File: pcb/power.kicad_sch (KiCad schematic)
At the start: 49 parts, among them U5 REG_LDO_3V3_250mA_TI_LP5907MF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, U7 REG_SW_BOOST_TI_TLV61046ADBV

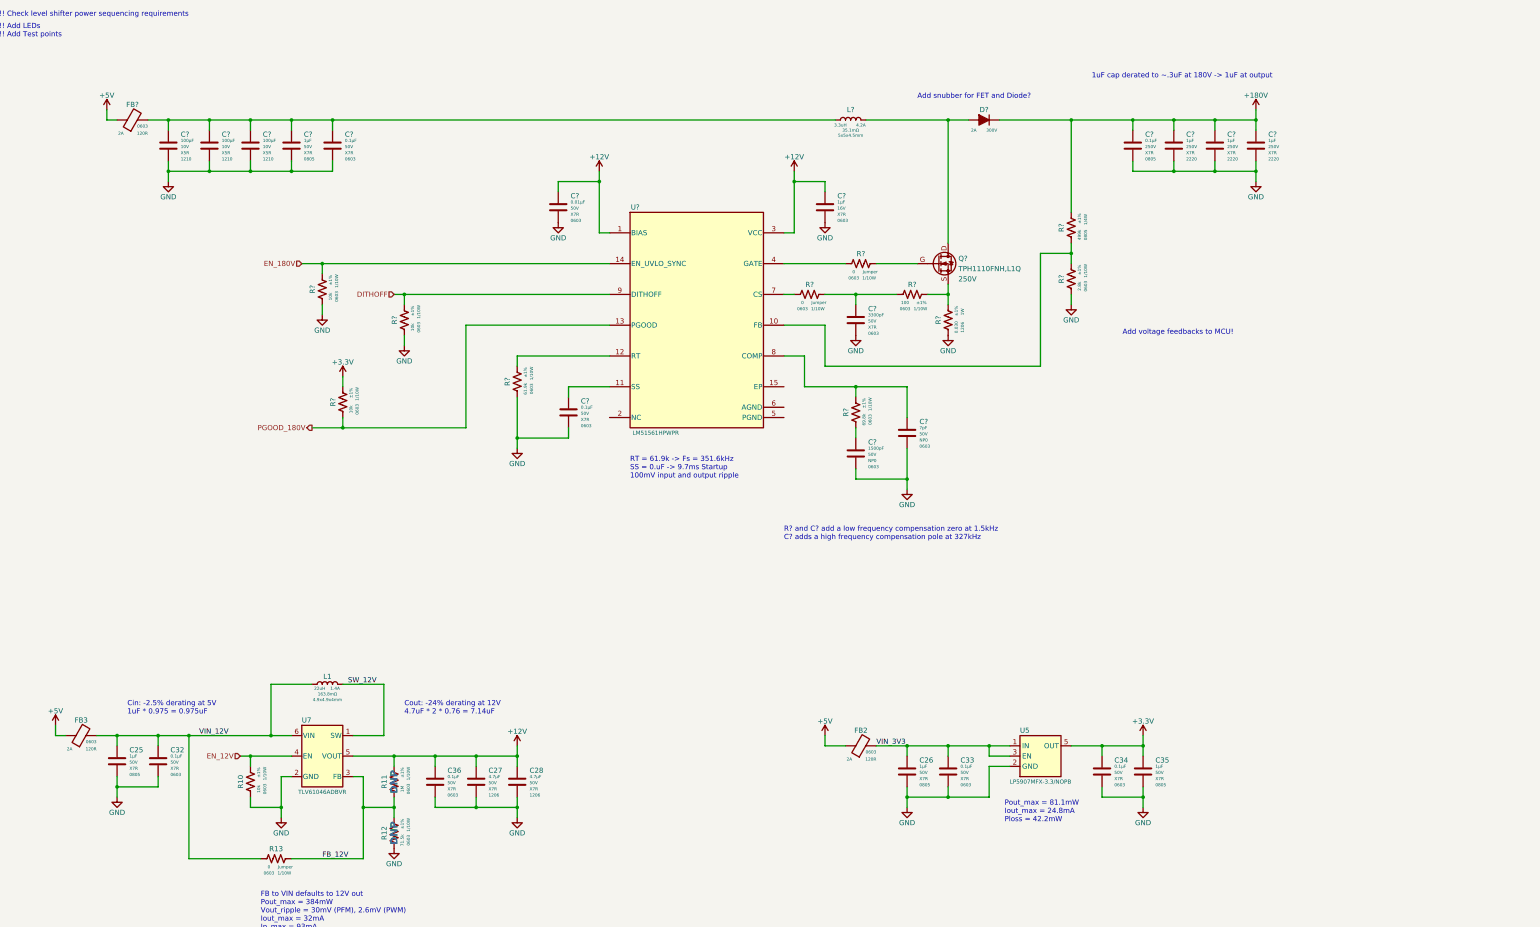
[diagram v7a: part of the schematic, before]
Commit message: Added snubber DNP footprints and named nets on power page.
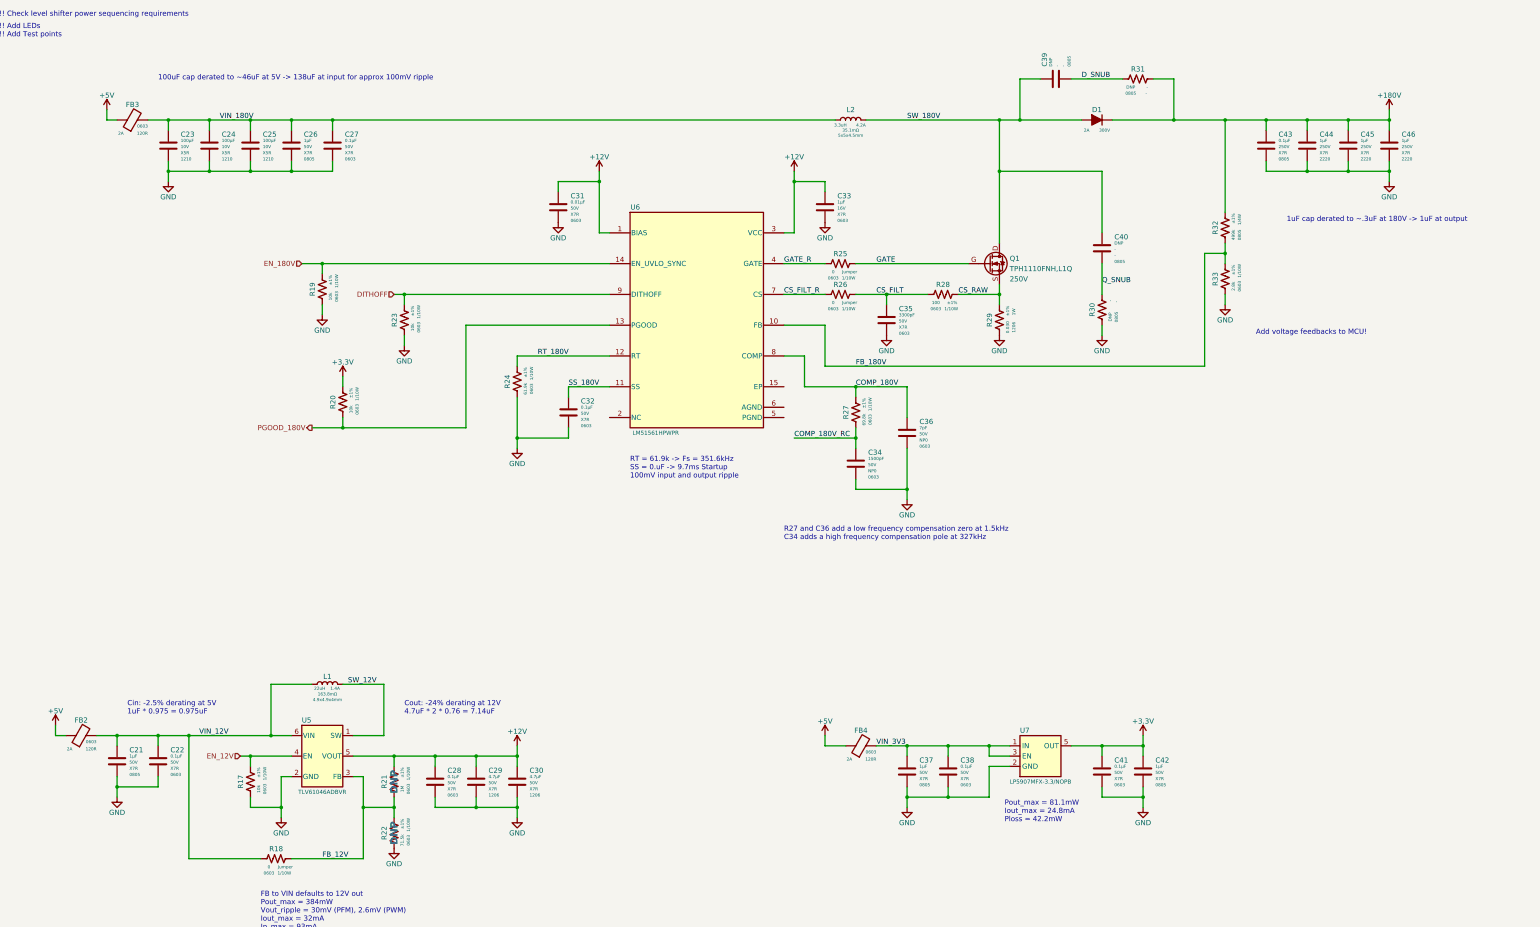
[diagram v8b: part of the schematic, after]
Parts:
- added C39, C40: CAP_CER_DNP_0805, Capacitor_SMD:C_0805_2012Metric, symbol .arjun:CAP_CER_DNP_0805
- added R30, R31: RES_DNP_0805, Resistor_SMD:R_0805_2012Metric, symbol .arjun:RES_DNP_0805
- L1: footprint arjun_footprints:L_Taiyo-Yuden_NR-50xx -> arjun_footprints:IND_Taiyo-Yuden_NR-50xx
- gave numbers to parts that had none: 31
- renumbered C25 to C21, C32 to C22, C36 to C28, C27 to C29, C28 to C30, C26 to C37, C33 to C38, C34 to C41, C35 to C42, FB3 to FB2, FB2 to FB4, R10 to R17, R13 to R18, R11 to R21, R12 to R22, U7 to U5, U5 to U7
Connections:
- net 180V: now also R31.1
- net GND: now also R30.2
- net RT_180V: now reaches R24.1, U6.12 (RT)
- net VIN_180V: now reaches C23.1, C24.1, C25.1, C26.1, C27.1, FB3.2, L2.1
- net CS_FILT: now reaches C35.1, R26.1, R28.2
- net SW_180V: now reaches D1.2 (A), L2.2, Q1.D
- net SW_180V: now also C39.1, C40.1
- net GATE: now reaches Q1.G, R25.1
- net CS_RAW: now reaches Q1.S, R28.1, R29.1
- net COMP_180V: now reaches C36.1, R27.1, U6.8 (COMP)
- net FB_180V: now reaches R32.2, R33.1, U6.10 (FB)
- net CS_FILT_R: now reaches R26.2, U6.7 (CS)
- net SS_180V: now reaches C32.1, U6.11 (SS)
- net GATE_R: now reaches R25.2, U6.4 (GATE)
- net COMP_180V_RC: now reaches C34.1, R27.2
- new net D_SNUB: C39.2, R31.2
- new net Q_SNUB: C40.2, R30.1
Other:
- note added: "100uF cap derated to ~46uF at 5V -> 138uF at input for approx 100mV ripple"
- note added: "R27 and C36 add a low frequency compensation zero at 1.5kHz C34 adds a high frequency compensation pole at 327kHz"
- note removed: "Add snubber for FET and Diode?"
- note removed: "R? and C? add a low frequency compensation zero at 1.5kHz C? adds a high frequency compensation pole at 327kHz"
- moved on the sheet: C34, C35, C43, C44, C45, C46, D1, Q1, R25, R26, R28, R29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
